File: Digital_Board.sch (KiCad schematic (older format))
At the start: 0 parts

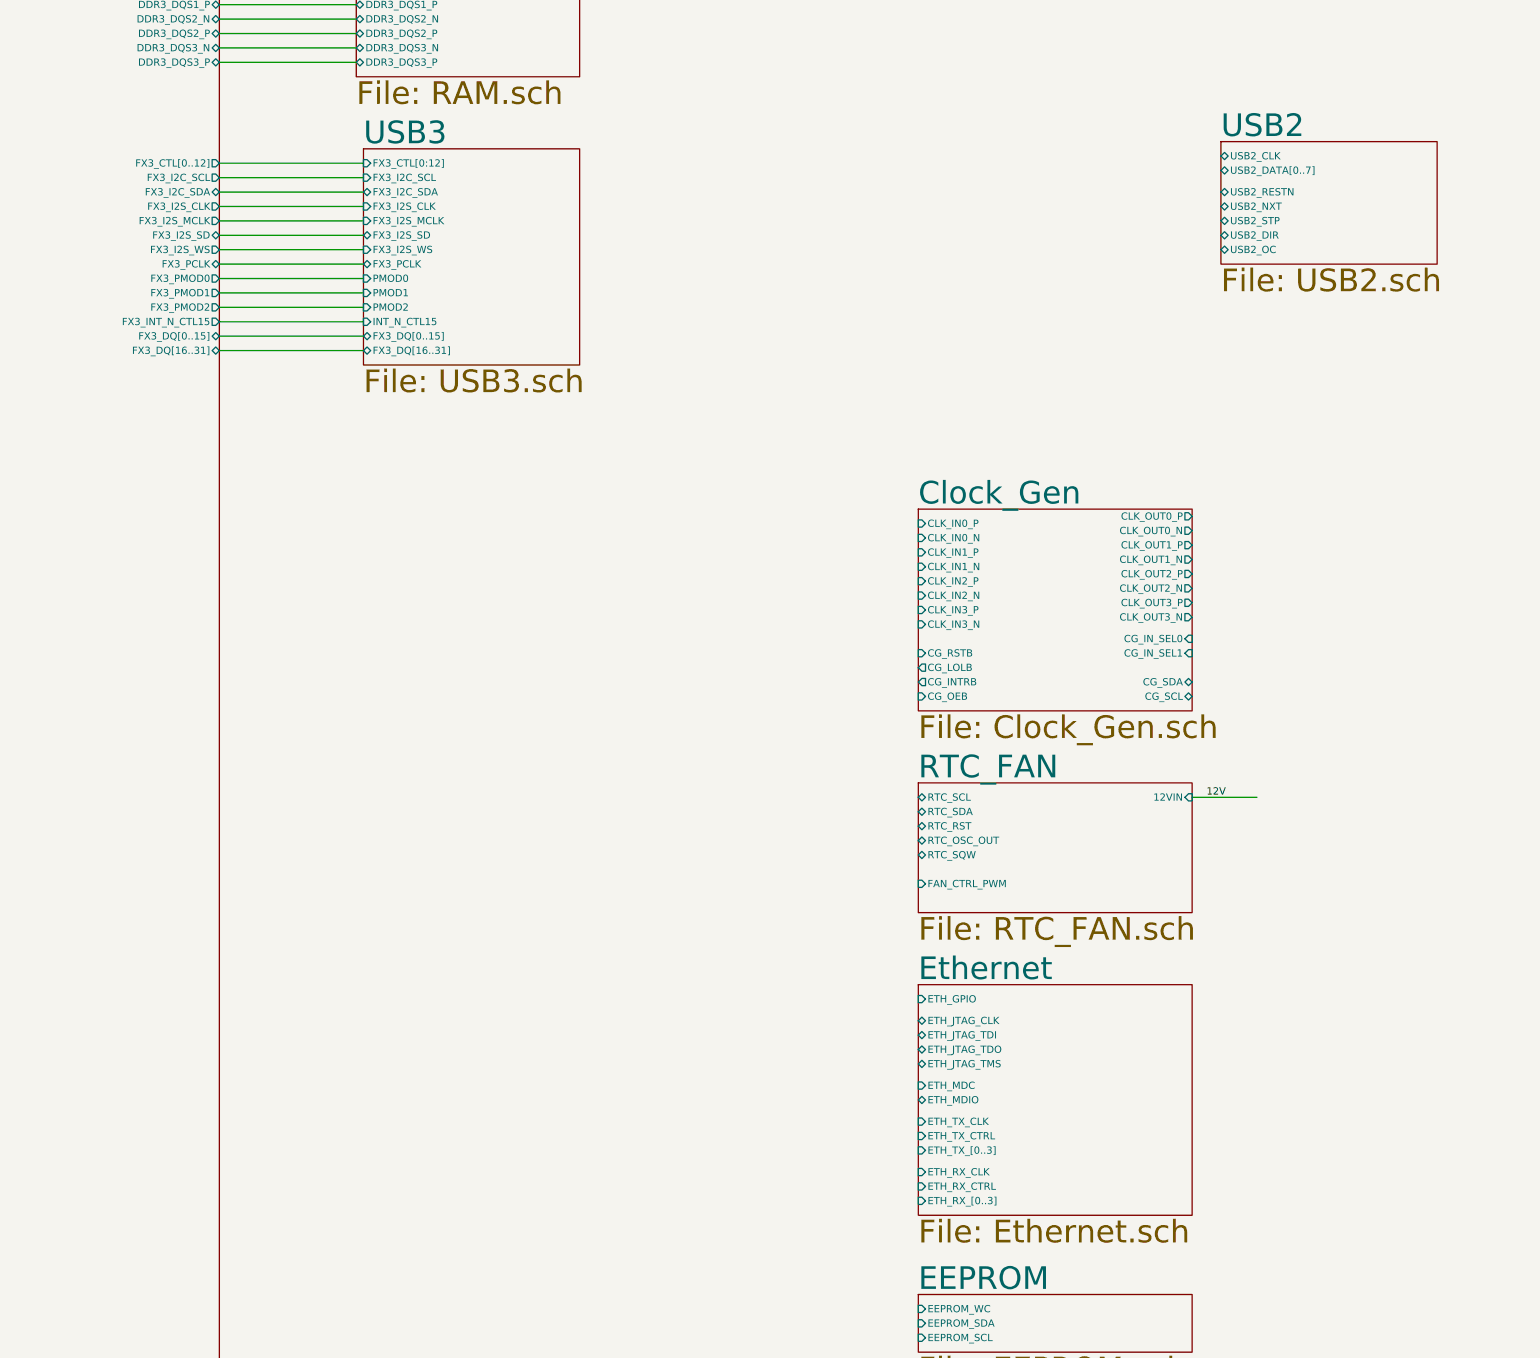
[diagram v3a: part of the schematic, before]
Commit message: Connected USB2 connections with FPGA and updated the top sheet
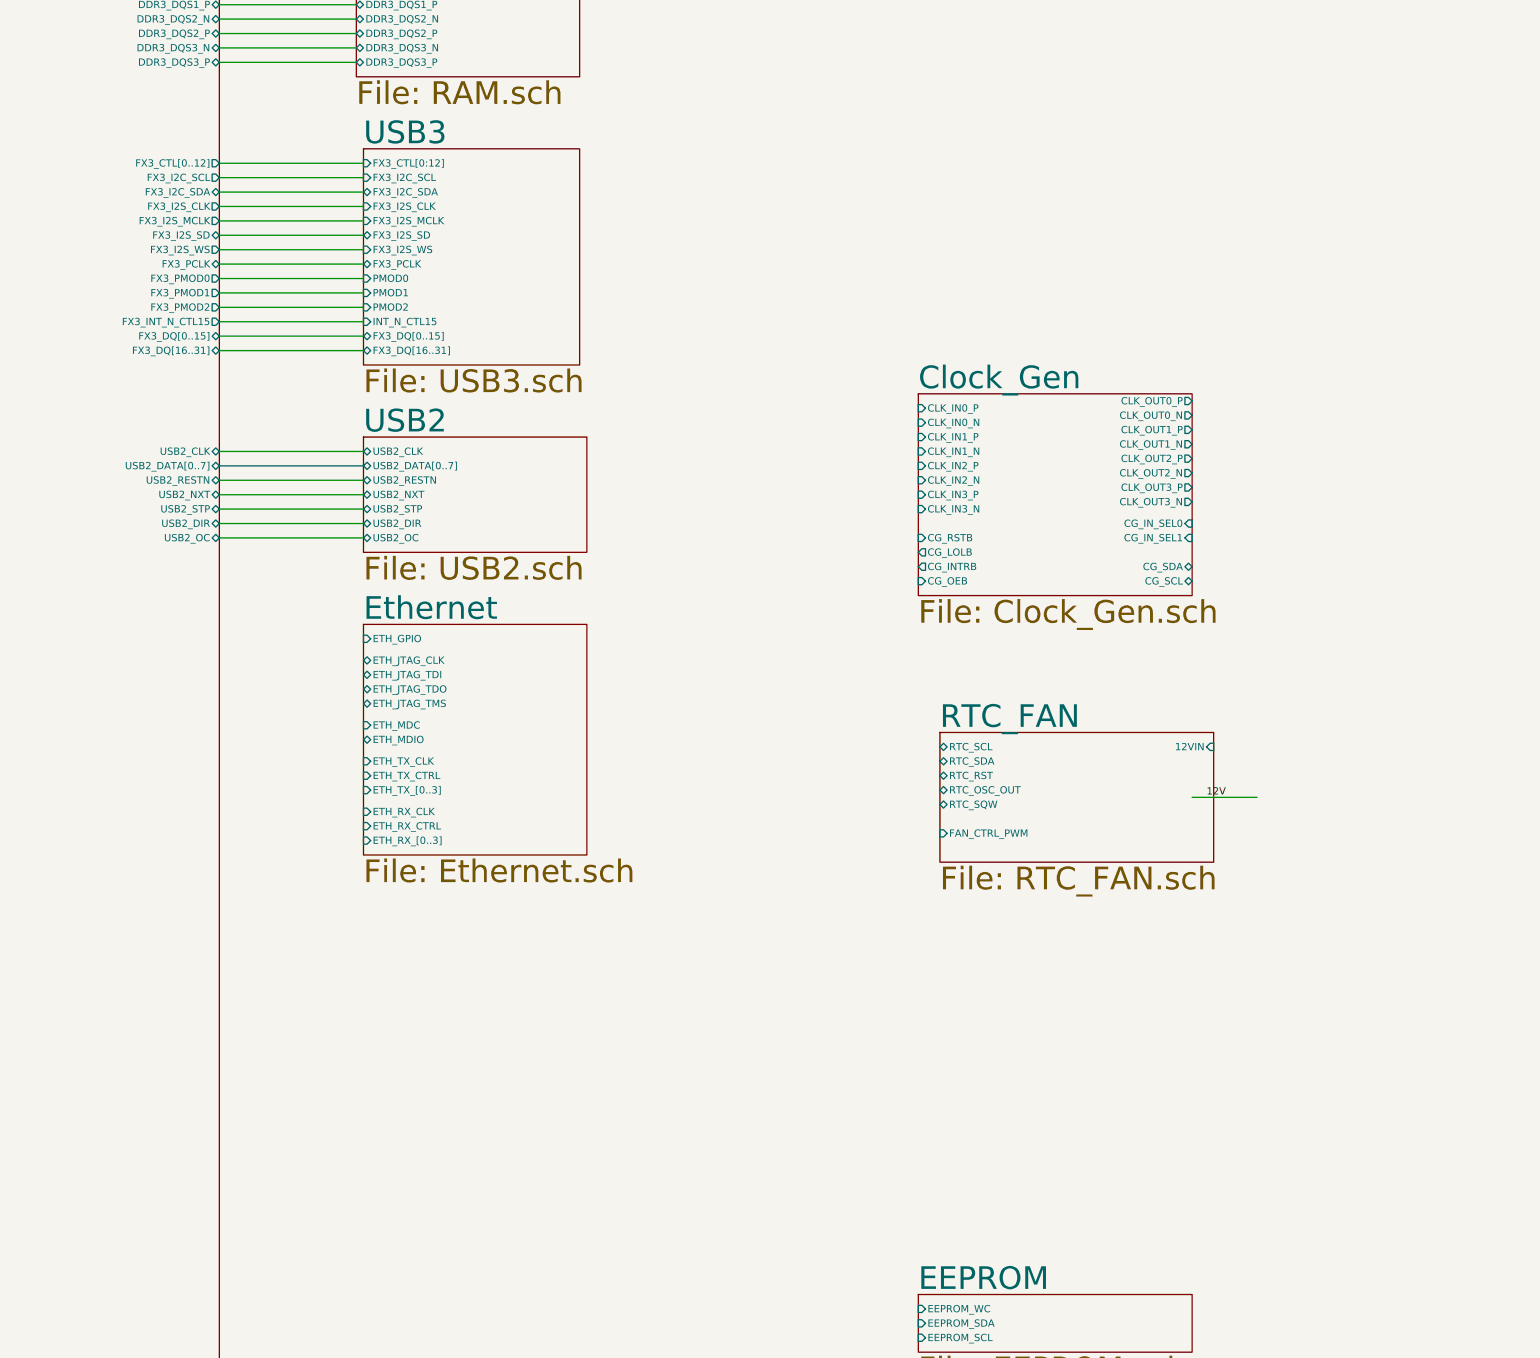
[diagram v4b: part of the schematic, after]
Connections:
- wire segments 38 -> 44
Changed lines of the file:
@@
 $EndSheet
 $Sheet
-S 19050 7800 1900 1400
+S 19050 7000 1900 1400
 U 601E7B38
 F0 "Clock_Gen" 157
 F1 "Clock_Gen.sch" 157
-F2 "CLK_IN0_P" I L 19050 7900 50
-F3 "CLK_IN0_N" I L 19050 8000 50
-F4 "CLK_IN1_P" I L 19050 8100 50
-F5 "CLK_IN1_N" I L 19050 8200 50
-F6 "CLK_IN2_P" I L 19050 8300 50
-F7 "CLK_IN2_N" I L 19050 8400 50
-F8 "CLK_IN3_P" I L 19050 8500 50
-F9 "CLK_IN3_N" I L 19050 8600 50
-F10 "CG_SDA" B R 20950 9000 50
-F11 "CG_SCL" B R 20950 9100 50
-F12 "CLK_OUT0_N" O R 20950 7950 50
-F13 "CLK_OUT0_P" O R 20950 7850 50
-F14 "CLK_OUT1_N" O R 20950 8150 50
-F15 "CLK_OUT1_P" O R 20950 8050 50
-F16 "CLK_OUT2_N" O R 20950 8350 50
-F17 "CLK_OUT2_P" O R 20950 8250 50
-F18 "CLK_OUT3_N" O R 20950 8550 50
-F19 "CLK_OUT3_P" O R 20950 8450 50
-F20 "CG_IN_SEL0" I R 20950 8700 50
-F21 "CG_IN_SEL1" I R 20950 8800 50
-F22 "CG_LOLB" O L 19050 8900 50
-F23 "CG_INTRB" O L 19050 9000 50
-F24 "CG_RSTB" I L 19050 8800 50
-F25 "CG_OEB" I L 19050 9100 50
+F2 "CLK_IN0_P" I L 19050 7100 50
+F3 "CLK_IN0_N" I L 19050 7200 50
+F4 "CLK_IN1_P" I L 19050 7300 50
+F5 "CLK_IN1_N" I L 19050 7400 50
+F6 "CLK_IN2_P" I L 19050 7500 50
+F7 "CLK_IN2_N" I L 19050 7600 50
+F8 "CLK_IN3_P" I L 19050 7700 50
+F9 "CLK_IN3_N" I L 19050 7800 50
+F10 "CG_SDA" B R 20950 8200 50
+F11 "CG_SCL" B R 20950 8300 50
+F12 "CLK_OUT0_N" O R 20950 7150 50
+F13 "CLK_OUT0_P" O R 20950 7050 50
+F14 "CLK_OUT1_N" O R 20950 7350 50
+F15 "CLK_OUT1_P" O R 20950 7250 50
+F16 "CLK_OUT2_N" O R 20950 7550 50
+F17 "CLK_OUT2_P" O R 20950 7450 50
+F18 "CLK_OUT3_N" O R 20950 7750 50
+F19 "CLK_OUT3_P" O R 20950 7650 50
+F20 "CG_IN_SEL0" I R 20950 7900 50
+F21 "CG_IN_SEL1" I R 20950 8000 50
+F22 "CG_LOLB" O L 19050 8100 50
+F23 "CG_INTRB" O L 19050 8200 50
+F24 "CG_RSTB" I L 19050 8000 50
+F25 "CG_OEB" I L 19050 8300 50
 $EndSheet
 $Sheet
@@
 $EndSheet
 $Sheet
-S 21150 5250 1500 850
+S 15200 7300 1550 800
 U 601E7BF0
 F0 "USB2" 157
 F1 "USB2.sch" 157
-F2 "USB2_DATA[0..7]" B L 21150 5450 50
-F3 "USB2_DIR" B L 21150 5900 50
-F4 "USB2_STP" B L 21150 5800 50
-F5 "USB2_NXT" B L 21150 5700 50
-F6 "USB2_RESTN" B L 21150 5600 50
-F7 "USB2_CLK" B L 21150 5350 50
-F8 "USB2_OC" B L 21150 6000 50
+F2 "USB2_DATA[0..7]" B L 15200 7500 50
+F3 "USB2_DIR" B L 15200 7900 50
+F4 "USB2_STP" B L 15200 7800 50
+F5 "USB2_NXT" B L 15200 7700 50
+F6 "USB2_RESTN" B L 15200 7600 50
+F7 "USB2_CLK" B L 15200 7400 50
+F8 "USB2_OC" B L 15200 8000 50
 $EndSheet
 $Sheet
@@
 $EndSheet
 $Sheet
-S 19050 11100 1900 1600
+S 15200 8600 1550 1600
 U 601E7C92
 F0 "Ethernet" 157
 F1 "Ethernet.sch" 157
-F2 "ETH_GPIO" I L 19050 11200 50
-F3 "ETH_JTAG_CLK" B L 19050 11350 50
-F4 "ETH_JTAG_TDI" B L 19050 11450 50
-F5 "ETH_JTAG_TDO" B L 19050 11550 50
-F6 "ETH_JTAG_TMS" B L 19050 11650 50
-F7 "ETH_MDC" I L 19050 11800 50
-F8 "ETH_MDIO" B L 19050 11900 50
-F9 "ETH_TX_CLK" I L 19050 12050 50
-F10 "ETH_TX_CTRL" I L 19050 12150 50
-F11 "ETH_TX_[0..3]" I L 19050 12250 50
-F12 "ETH_RX_[0..3]" I L 19050 12600 50
-F13 "ETH_RX_CLK" I L 19050 12400 50
-F14 "ETH_RX_CTRL" I L 19050 12500 50
-$EndSheet
-$Sheet
-S 19050 9700 1900 900
+F2 "ETH_GPIO" I L 15200 8700 50
+F3 "ETH_JTAG_CLK" B L 15200 8850 50
+F4 "ETH_JTAG_TDI" B L 15200 8950 50
+F5 "ETH_JTAG_TDO" B L 15200 9050 50
+F6 "ETH_JTAG_TMS" B L 15200 9150 50
+F7 "ETH_MDC" I L 15200 9300 50
+F8 "ETH_MDIO" B L 15200 9400 50
+F9 "ETH_TX_CLK" I L 15200 9550 50
+F10 "ETH_TX_CTRL" I L 15200 9650 50
+F11 "ETH_TX_[0..3]" I L 15200 9750 50
+F12 "ETH_RX_[0..3]" I L 15200 10100 50
+F13 "ETH_RX_CLK" I L 15200 9900 50
+F14 "ETH_RX_CTRL" I L 15200 10000 50
+$EndSheet
+$Sheet
+S 19200 9350 1900 900
 U 601E7CC8
 F0 "RTC_FAN" 157
 F1 "RTC_FAN.sch" 157
-F2 "RTC_SCL" B L 19050 9800 50
-F3 "RTC_SDA" B L 19050 9900 50
-F4 "RTC_RST" B L 19050 10000 50
-F5 "RTC_OSC_OUT" B L 19050 10100 50
-F6 "RTC_SQW" B L 19050 10200 50
-F7 "FAN_CTRL_PWM" I L 19050 10400 50
-F8 "12VIN" I R 20950 9800 50
+F2 "RTC_SCL" B L 19200 9450 50
+F3 "RTC_SDA" B L 19200 9550 50
+F4 "RTC_RST" B L 19200 9650 50
+F5 "RTC_OSC_OUT" B L 19200 9750 50
+F6 "RTC_SQW" B L 19200 9850 50
+F7 "FAN_CTRL_PWM" I L 19200 10050 50
+F8 "12VIN" I R 21100 9450 50
 $EndSheet
 $Sheet
@@
 F40 "FX3_CTL[0..12]" O R 14200 5400 50
 F41 "FX3_INT_N_CTL15" O R 14200 6500 50
+F42 "USB2_DATA[0..7]" B R 14200 7500 50
+F43 "USB2_DIR" B R 14200 7900 50
+F44 "USB2_STP" B R 14200 7800 50
+F45 "USB2_NXT" B R 14200 7700 50
+F46 "USB2_CLK" B R 14200 7400 50
+F47 "USB2_RESTN" B R 14200 7600 50
+F48 "USB2_OC" B R 14200 8000 50
 $EndSheet
 Text Label 3650 14750 0    50   ~ 0
@@
 Wire Wire Line
 	14200 6700 15200 6700
+Wire Bus Line
+	15200 7500 14200 7500
+Wire Wire Line
+	15200 7400 14200 7400
+Wire Wire Line
+	14200 7600 15200 7600
+Wire Wire Line
+	15200 7700 14200 7700
+Wire Wire Line
+	14200 7800 15200 7800
+Wire Wire Line
+	15200 7900 14200 7900
+Wire Wire Line
+	14200 8000 15200 8000
 $EndSCHEMATC

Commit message: Added ADC schematic
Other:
- note added: "put filter beads for all power supplies at each circuit"
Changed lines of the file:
@@
 $Descr A2 23386 16535
 encoding utf-8
-Sheet 1 22
+Sheet 1 25
 Title "CGMPCX1006"
 Date "2021-02-03"
@@
 S 1600 9200 2300 1900
 U 605FDA0D
-F0 "ADC" 50
-F1 "ADC.sch" 50
+F0 "ADC" 100
+F1 "ADC.sch" 100
 $EndSheet
 $Sheet
@@
 Wire Wire Line
 	14200 8000 15200 8000
+Text Notes 15850 950  0    157  ~ 0
+put filter beads for all power supplies at each circuit
 $EndSCHEMATC

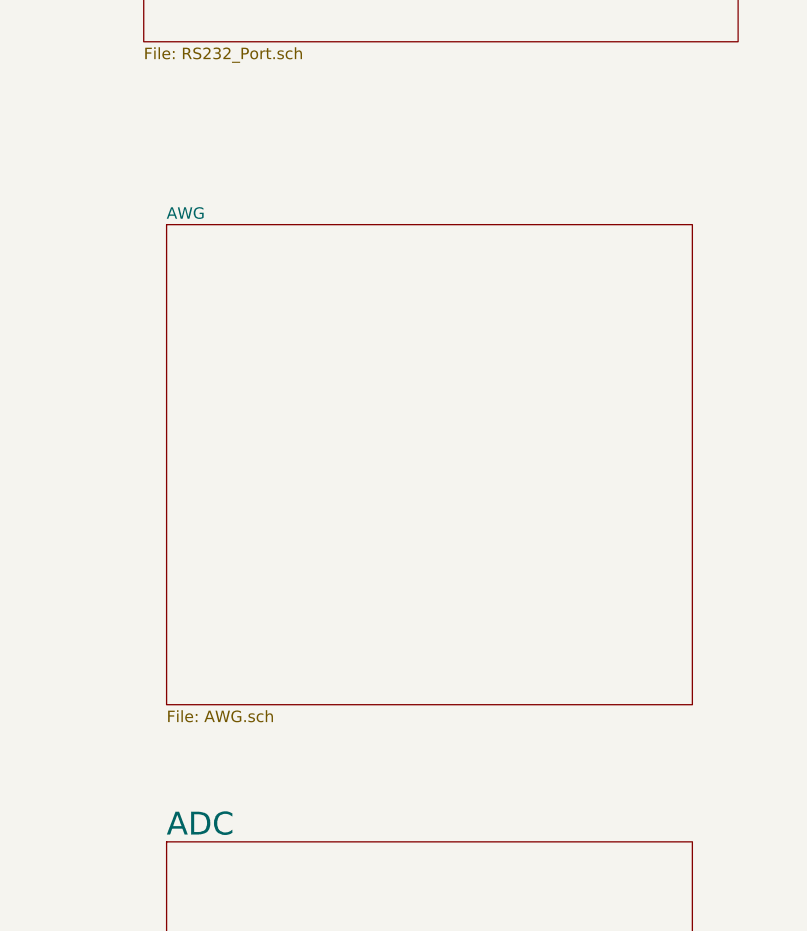
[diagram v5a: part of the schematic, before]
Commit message: Added Fast DAC schematic
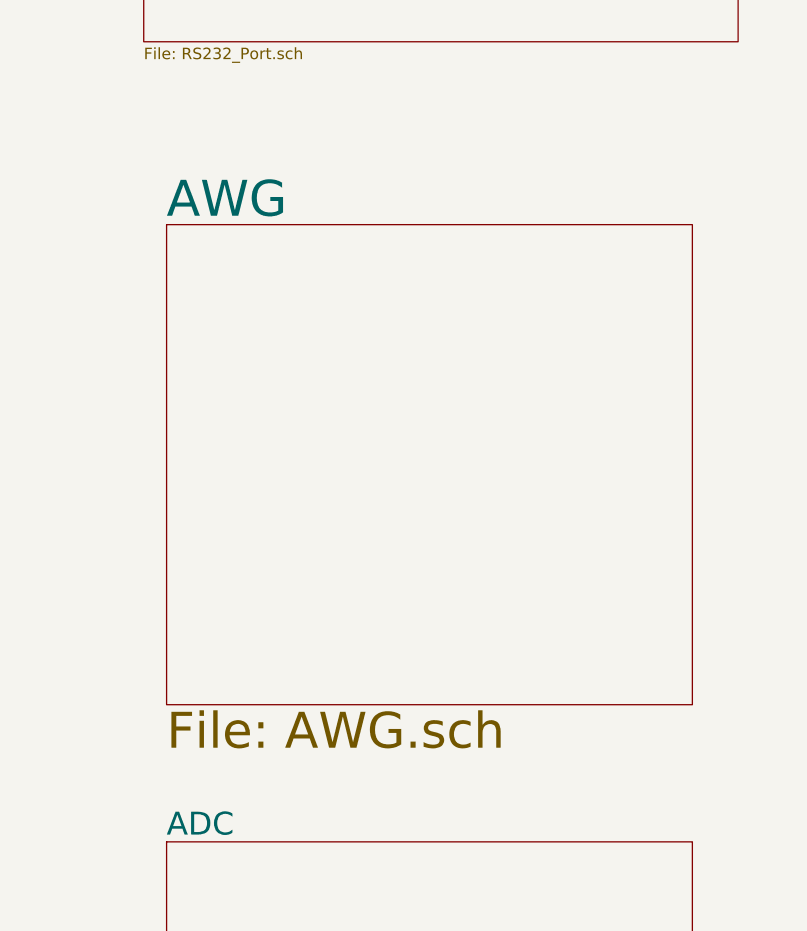
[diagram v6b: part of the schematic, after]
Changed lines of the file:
@@
 S 1600 6500 2300 2100
 U 605FD9FD
-F0 "AWG" 50
-F1 "AWG.sch" 50
+F0 "AWG" 157
+F1 "AWG.sch" 157
 $EndSheet
 $Sheet
